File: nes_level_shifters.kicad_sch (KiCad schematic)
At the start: 18 parts, among them J2 NES 3v3 TP, U1 74ALVC164245, U2 74ALVC164245, U3 74ALVC164245, U4 74ALVC164245

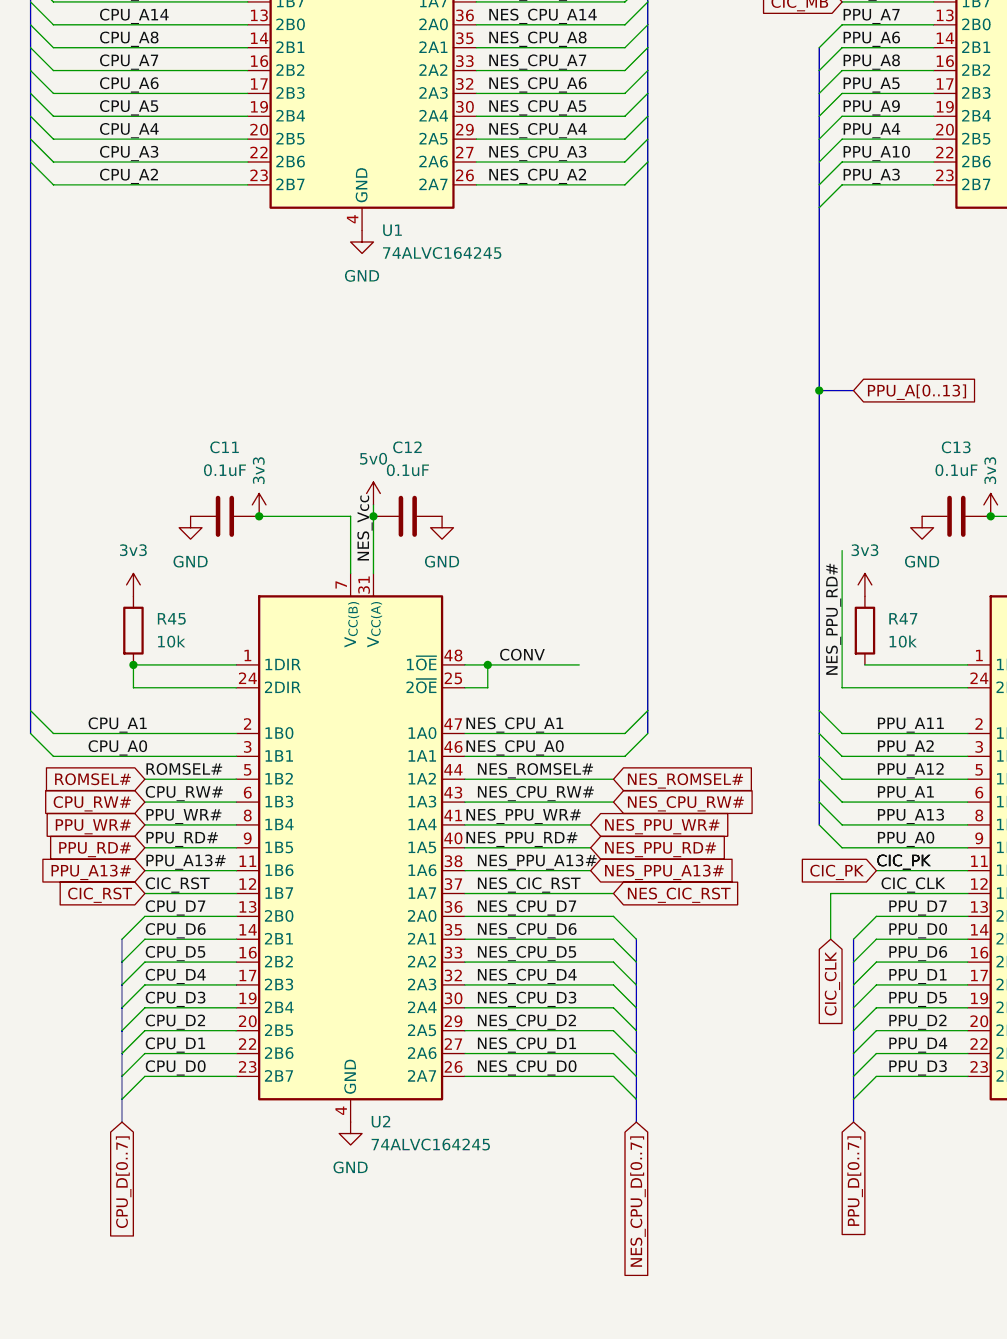
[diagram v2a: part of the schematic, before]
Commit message: Re-do the board layout
Signed-off-by: Chris Frantz <frantzcj@gmail.com>
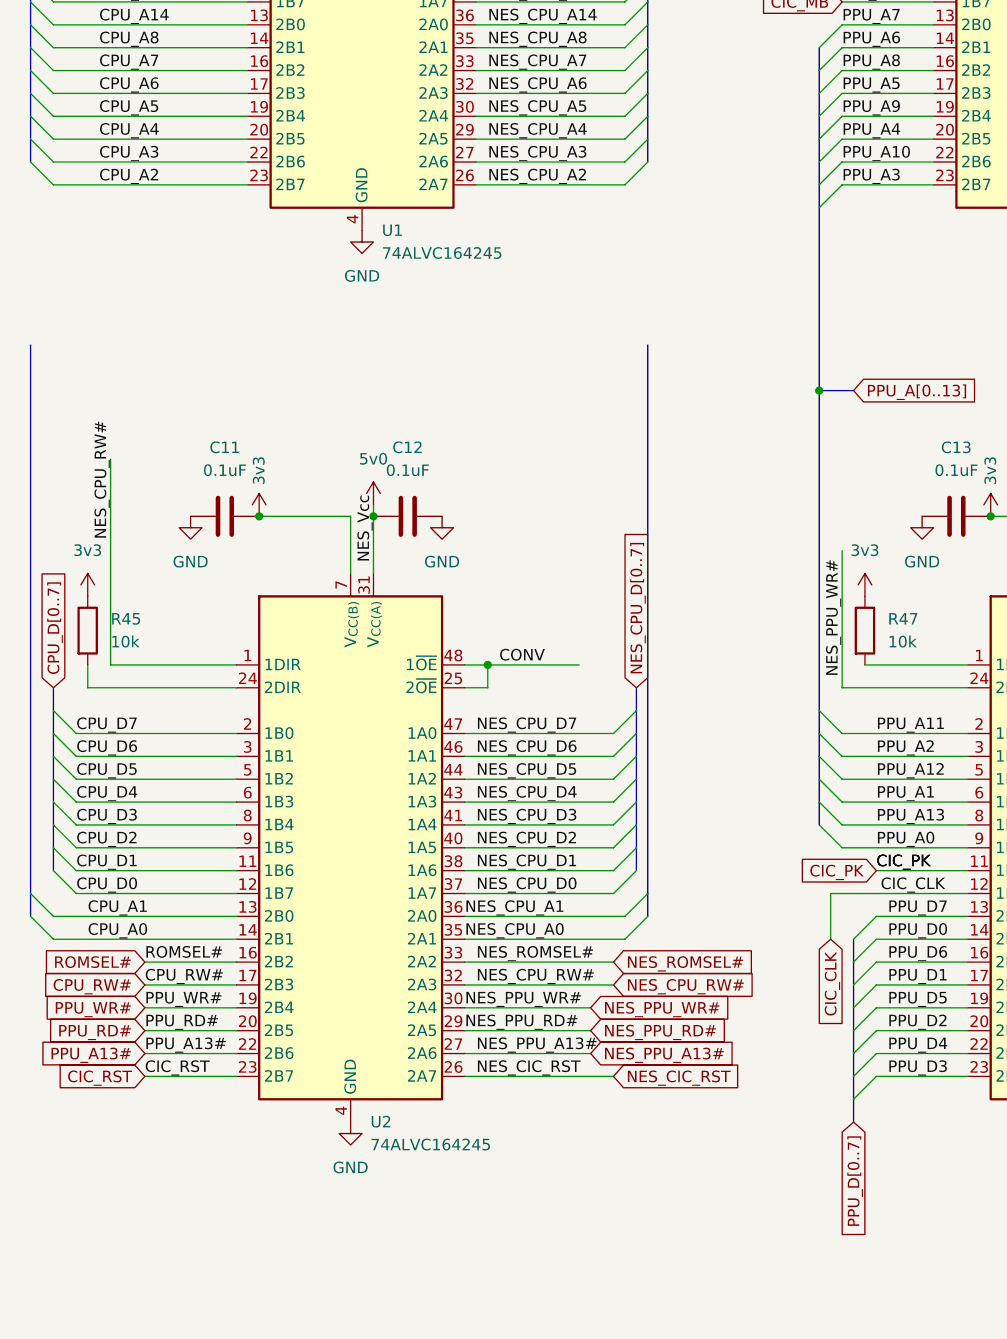
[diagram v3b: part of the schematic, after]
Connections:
- net CIC_RST: now also U2.23 (2B7); no longer U2.12 (1B7)
- net CPU_A0: now also U2.14 (2B1); no longer U2.3 (1B1)
- net CPU_A1: now also U2.13 (2B0); no longer U2.2 (1B0)
- net CPU_D0: now also U2.12 (1B7); no longer U2.23 (2B7)
- net CPU_D1: now also U2.11 (1B6); no longer U2.22 (2B6)
- net CPU_D2: now also U2.9 (1B5); no longer U2.20 (2B5)
- net CPU_D3: now also U2.8 (1B4); no longer U2.19 (2B4)
- net CPU_D4: now also U2.6 (1B3); no longer U2.17 (2B3)
- net CPU_D5: now also U2.5 (1B2); no longer U2.16 (2B2)
- net CPU_D6: now also U2.3 (1B1); no longer U2.14 (2B1)
- net CPU_D7: now also U2.2 (1B0); no longer U2.13 (2B0)
- net CPU_RW#: now also U2.17 (2B3); no longer U2.6 (1B3)
- net NES_CIC_RST: now also U2.26 (2A7); no longer U2.37 (1A7)
- net NES_CPU_A0: now also U2.35 (2A1); no longer U2.46 (1A1)
- net NES_CPU_A1: now also U2.36 (2A0); no longer U2.47 (1A0)
- net NES_CPU_D0: now also U2.37 (1A7); no longer U2.26 (2A7)
- net NES_CPU_D1: now also U2.38 (1A6); no longer U2.27 (2A6)
- net NES_CPU_D2: now also U2.40 (1A5); no longer U2.29 (2A5)
- net NES_CPU_D3: now also U2.41 (1A4); no longer U2.30 (2A4)
- net NES_CPU_D4: now also U2.43 (1A3); no longer U2.32 (2A3)
- net NES_CPU_D5: now also U2.44 (1A2); no longer U2.33 (2A2)
- net NES_CPU_D6: now also U2.46 (1A1); no longer U2.35 (2A1)
- net NES_CPU_D7: now also U2.47 (1A0); no longer U2.36 (2A0)
- net NES_CPU_RW#: now also U2.1 (1DIR), U2.32 (2A3); no longer U2.43 (1A3)
- net NES_PPU_A13#: now also U2.27 (2A6); no longer U2.38 (1A6)
- net NES_PPU_RD#: now also U2.29 (2A5); no longer U2.40 (1A5), U4.24 (2DIR)
- net NES_PPU_WR#: now also U2.30 (2A4), U4.24 (2DIR); no longer U2.41 (1A4)
- net NES_ROMSEL#: now also U2.33 (2A2); no longer U2.44 (1A2)
- net PPU_A13#: now also U2.22 (2B6); no longer U2.11 (1B6)
- net PPU_RD#: now also U2.20 (2B5); no longer U2.9 (1B5)
- net PPU_WR#: now also U2.19 (2B4); no longer U2.8 (1B4)
- net ROMSEL#: now also U2.16 (2B2); no longer U2.5 (1B2)
- net at R45.2, U2.24 (2DIR): no longer U2.1 (1DIR)
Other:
- moved on the sheet: R45
